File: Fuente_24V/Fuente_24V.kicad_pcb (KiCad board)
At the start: 2 copper layers, 83.5 x 71 mm, 10 parts, among them J1 Screw_Terminal_01x03, J2 Screw_Terminal_01x02

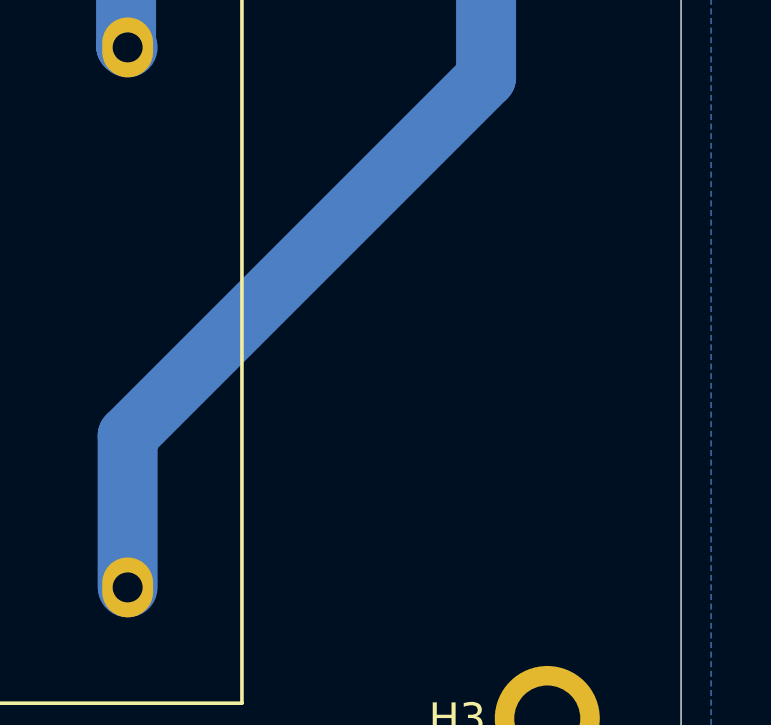
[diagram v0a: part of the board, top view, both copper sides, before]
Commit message: se agrega led indicador de fuente al esquema
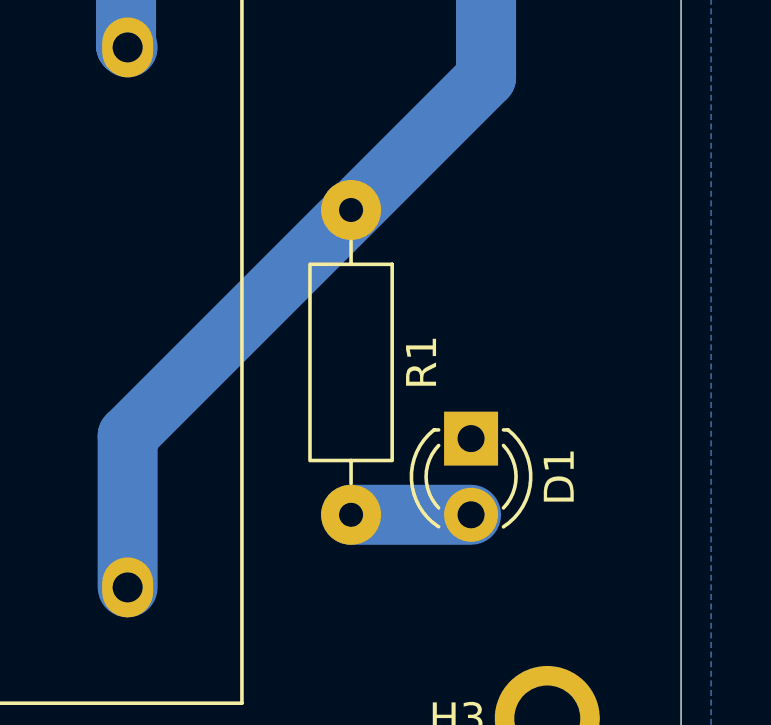
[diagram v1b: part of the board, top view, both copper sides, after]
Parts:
- added D1: LED, LED_THT:LED_D3.0mm, F.Cu at (127.0, 93.5)
- added R1: R, Resistor_THT:R_Axial_DIN0207_L6.3mm_D2.5mm_P10.16mm_Horizontal, F.Cu at (123.0, 85.9)
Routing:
- net Net-(D1-A): track 0.00 -> 4.00 mm
